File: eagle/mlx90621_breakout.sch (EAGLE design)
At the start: 16 parts, among them J1 ARDUINO_R3_SHIELD

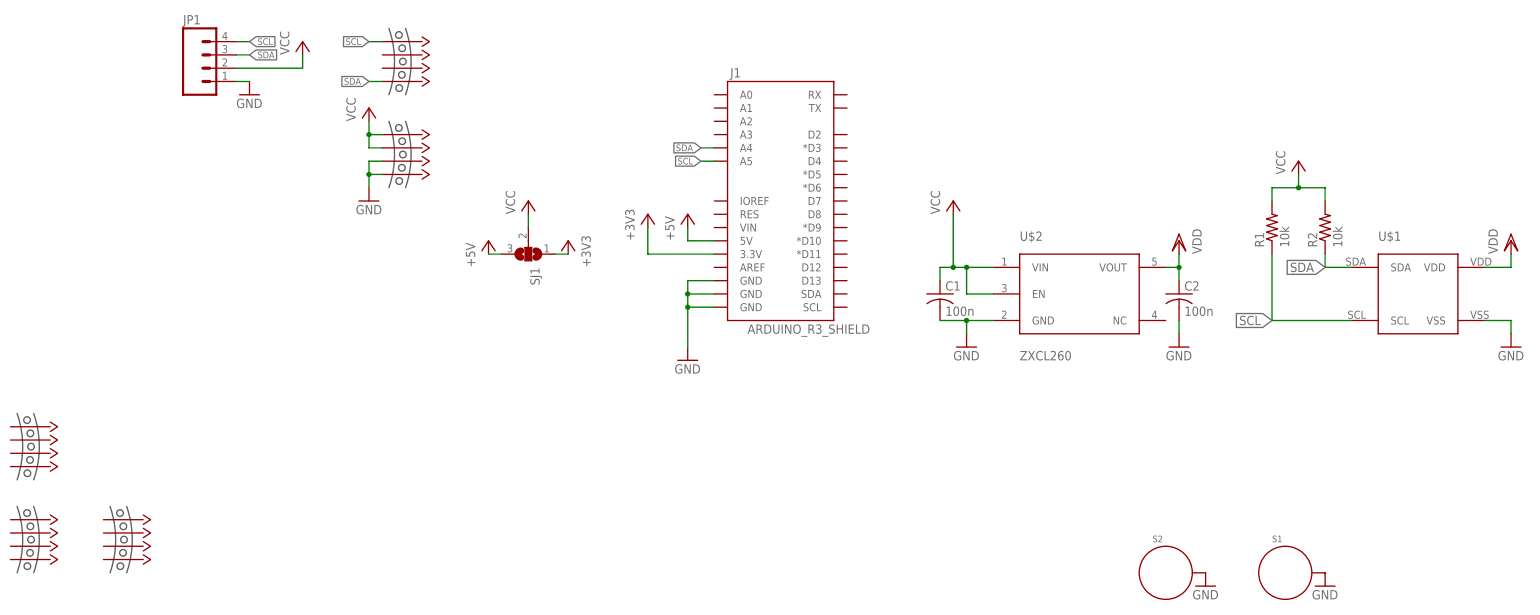
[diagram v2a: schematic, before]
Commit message: cleaned PCB (Removed shield)
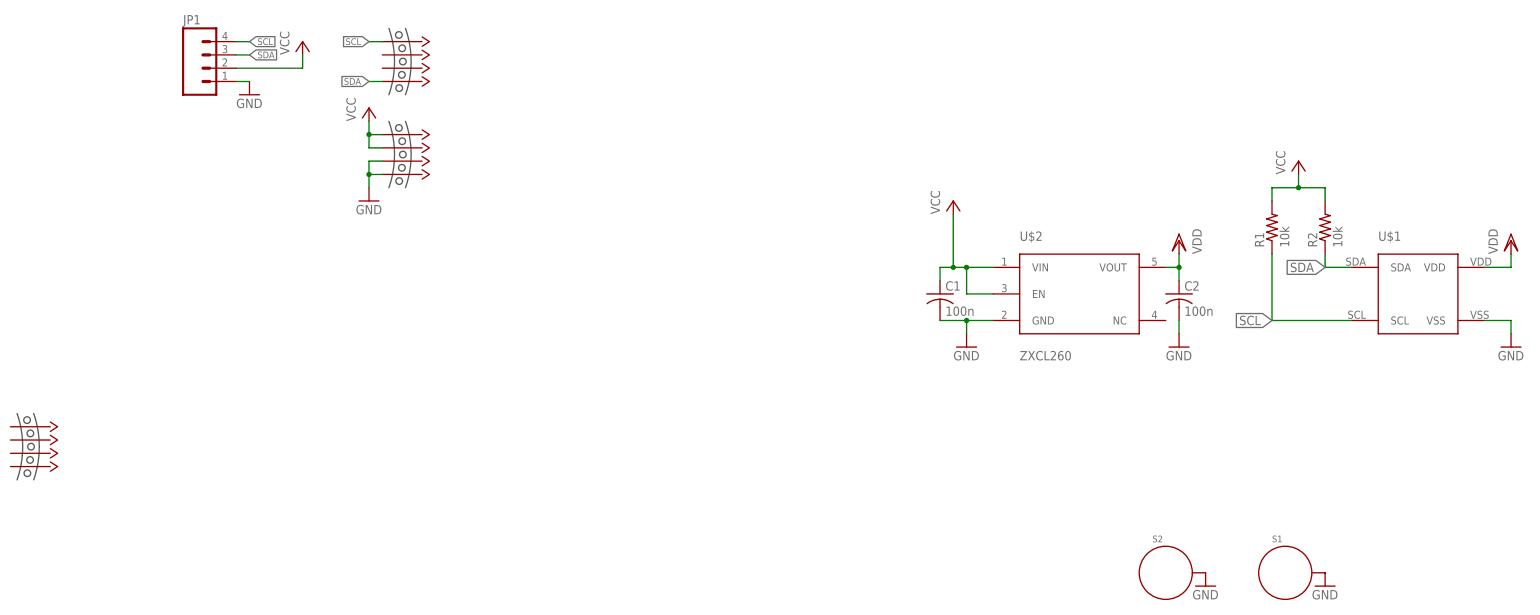
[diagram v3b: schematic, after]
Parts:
- removed J1: ARDUINO_R3_SHIELD, SparkFun-Boards:ARDUINO_R3_SHIELD
- removed SJ1: (no value), jumper:SJ2W
- removed U$6, U$7: MOUSE-BITES-4, mouse-bites:MOUSE-BITES-4
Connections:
- removed net +3V3: J1.3.3V, SJ1.1
- removed net +5V: J1.5V, SJ1.3
- net GND: no longer J1.GND@0, J1.GND@1, J1.GND@2
- net SCL: no longer J1.A5
- net SDA: no longer J1.A4
- net VCC: no longer SJ1.2
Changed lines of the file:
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@@
 <?xml version="1.0" encoding="utf-8"?>
 <!DOCTYPE eagle SYSTEM "eagle.dtd">
-<eagle version="7.3.0">
+<eagle version="9.0.1">
 <drawing>
 <settings>
 <setting alwaysvectorfont="no"/>
+<setting keepoldvectorfont="yes"/>
 <setting verticaltext="up"/>
 </settings>
@@
 </classes>
 <parts>
-<part name="J1" library="SparkFun-Boards" deviceset="ARDUINO_R3_SHIELD" device=""/>
 <part name="FRAME1" library="frames" deviceset="A3L-LOC" device=""/>
 <part name="C1" library="adafruit" deviceset="C-US" device="C0603" value="100n"/>
@@
 <part name="VDD2" library="supply1" deviceset="VDD" device=""/>
 <part name="GND3" library="SparkFun-Aesthetics" deviceset="GND" device=""/>
-<part name="P+3" library="supply1" deviceset="VCC" device=""/>
-<part name="GND4" library="SparkFun-Aesthetics" deviceset="GND" device=""/>
-<part name="SJ1" library="jumper" deviceset="SJ2W" device=""/>
-<part name="P+4" library="supply1" deviceset="+5V" device=""/>
-<part name="P+5" library="supply1" deviceset="+5V" device=""/>
-<part name="+3V1" library="supply1" deviceset="+3V3" device=""/>
-<part name="+3V2" library="supply1" deviceset="+3V3" device=""/>
 <part name="S1" library="SparkFun-Electromechanical" deviceset="STANDOFF_ELECTRICAL" device=""/>
 <part name="S2" library="SparkFun-Electromechanical" deviceset="STANDOFF_ELECTRICAL" device=""/>
@@
 <part name="P+7" library="supply1" deviceset="VCC" device=""/>
 <part name="U$5" library="mouse-bites" deviceset="MOUSE-BITES-4" device=""/>
-<part name="U$6" library="mouse-bites" deviceset="MOUSE-BITES-4" device=""/>
-<part name="U$7" library="mouse-bites" deviceset="MOUSE-BITES-4" device=""/>
 </parts>
 <sheets>
@@
 </plain>
 <instances>
-<instance part="J1" gate="G$1" x="228.6" y="86.36"/>
 <instance part="FRAME1" gate="G$1" x="0" y="0"/>
 <instance part="C1" gate="G$1" x="259.08" y="66.04"/>
@@
 <instance part="VDD2" gate="G$1" x="368.3" y="76.2"/>
 <instance part="GND3" gate="1" x="368.3" y="55.88"/>
-<instance part="P+3" gate="VCC" x="180.34" y="83.82"/>
-<instance part="GND4" gate="1" x="210.82" y="53.34"/>
-<instance part="SJ1" gate="G$1" x="180.34" y="73.66" rot="R270"/>
-<instance part="P+4" gate="1" x="172.72" y="76.2"/>
-<instance part="P+5" gate="1" x="210.82" y="81.28"/>
-<instance part="+3V1" gate="G$1" x="187.96" y="76.2" rot="MR0"/>
-<instance part="+3V2" gate="G$1" x="203.2" y="81.28"/>
 <instance part="S1" gate="G$1" x="325.12" y="12.7"/>
 <instance part="S2" gate="G$1" x="302.26" y="12.7"/>
@@
 <instance part="P+7" gate="VCC" x="149.86" y="101.6"/>
 <instance part="U$5" gate="G$1" x="81.28" y="43.18"/>
-<instance part="U$6" gate="G$1" x="81.28" y="25.4"/>
-<instance part="U$7" gate="G$1" x="99.06" y="25.4"/>
 </instances>
 <busses>
@@
 <wire x1="363.22" y1="60.96" x2="368.3" y2="60.96" width="0.1524" layer="91"/>
 <wire x1="368.3" y1="60.96" x2="368.3" y2="58.42" width="0.1524" layer="91"/>
-</segment>
-<segment>
-<pinref part="J1" gate="G$1" pin="GND@0"/>
-<pinref part="GND4" gate="1" pin="GND"/>
-<wire x1="215.9" y1="63.5" x2="210.82" y2="63.5" width="0.1524" layer="91"/>
-<wire x1="210.82" y1="63.5" x2="210.82" y2="55.88" width="0.1524" layer="91"/>
-<pinref part="J1" gate="G$1" pin="GND@1"/>
-<wire x1="215.9" y1="66.04" x2="210.82" y2="66.04" width="0.1524" layer="91"/>
-<wire x1="210.82" y1="66.04" x2="210.82" y2="63.5" width="0.1524" layer="91"/>
-<junction x="210.82" y="63.5"/>
-<pinref part="J1" gate="G$1" pin="GND@2"/>
-<wire x1="215.9" y1="68.58" x2="210.82" y2="68.58" width="0.1524" layer="91"/>
-<wire x1="210.82" y1="68.58" x2="210.82" y2="66.04" width="0.1524" layer="91"/>
-<junction x="210.82" y="66.04"/>
 </segment>
 <segment>
@@
 </segment>
 <segment>
-<pinref part="SJ1" gate="G$1" pin="2"/>
-<pinref part="P+3" gate="VCC" pin="VCC"/>
-<wire x1="180.34" y1="81.28" x2="180.34" y2="78.74" width="0.1524" layer="91"/>
-</segment>
-<segment>
 <pinref part="JP1" gate="G$1" pin="2"/>
 <wire x1="124.46" y1="109.22" x2="137.16" y2="109.22" width="0.1524" layer="91"/>
@@
 </segment>
 <segment>
-<pinref part="J1" gate="G$1" pin="A4"/>
-<wire x1="215.9" y1="93.98" x2="213.36" y2="93.98" width="0.1524" layer="91"/>
-<label x="213.36" y="93.98" size="1.27" layer="95" rot="R180" xref="yes"/>
-</segment>
-<segment>
 <pinref part="JP1" gate="G$1" pin="3"/>
 <wire x1="124.46" y1="111.76" x2="127" y2="111.76" width="0.1524" layer="91"/>
@@
 </segment>
 <segment>
-<pinref part="J1" gate="G$1" pin="A5"/>
-<wire x1="215.9" y1="91.44" x2="213.36" y2="91.44" width="0.1524" layer="91"/>
-<label x="213.36" y="91.44" size="1.27" layer="95" rot="R180" xref="yes"/>
-</segment>
-<segment>
 <pinref part="JP1" gate="G$1" pin="4"/>
 <wire x1="124.46" y1="114.3" x2="127" y2="114.3" width="0.1524" layer="91"/>
@@
 </segment>
 </net>
-<net name="+3V3" class="0">
-<segment>
-<pinref part="J1" gate="G$1" pin="3.3V"/>
-<pinref part="+3V2" gate="G$1" pin="+3V3"/>
-<wire x1="203.2" y1="78.74" x2="203.2" y2="73.66" width="0.1524" layer="91"/>
-<wire x1="203.2" y1="73.66" x2="215.9" y2="73.66" width="0.1524" layer="91"/>
-</segment>
-<segment>
-<pinref part="SJ1" gate="G$1" pin="1"/>
-<pinref part="+3V1" gate="G$1" pin="+3V3"/>
-<wire x1="187.96" y1="73.66" x2="185.42" y2="73.66" width="0.1524" layer="91"/>
-</segment>
-</net>
-<net name="+5V" class="0">
-<segment>
-<pinref part="SJ1" gate="G$1" pin="3"/>
-<pinref part="P+4" gate="1" pin="+5V"/>
-<wire x1="172.72" y1="73.66" x2="175.26" y2="73.66" width="0.1524" layer="91"/>
-</segment>
-<segment>
-<pinref part="J1" gate="G$1" pin="5V"/>
-<pinref part="P+5" gate="1" pin="+5V"/>
-<wire x1="210.82" y1="78.74" x2="210.82" y2="76.2" width="0.1524" layer="91"/>
-<wire x1="210.82" y1="76.2" x2="215.9" y2="76.2" width="0.1524" layer="91"/>
-</segment>
-</net>
